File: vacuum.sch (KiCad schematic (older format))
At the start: 28 parts, among them J1 нагрузка, J2 нагрузка, J3 нагрузка, J4 геркон клапана 0, J5 геркон клапана 1, J6 геркон шибера 0, J7 геркон шибера 1, Q1 IRF740, Q2 IRF740, Q3 IRF740, SW1 Кнопка, SW2 Кнопка, SW3 Кнопка, SW4 Выключить автоматику

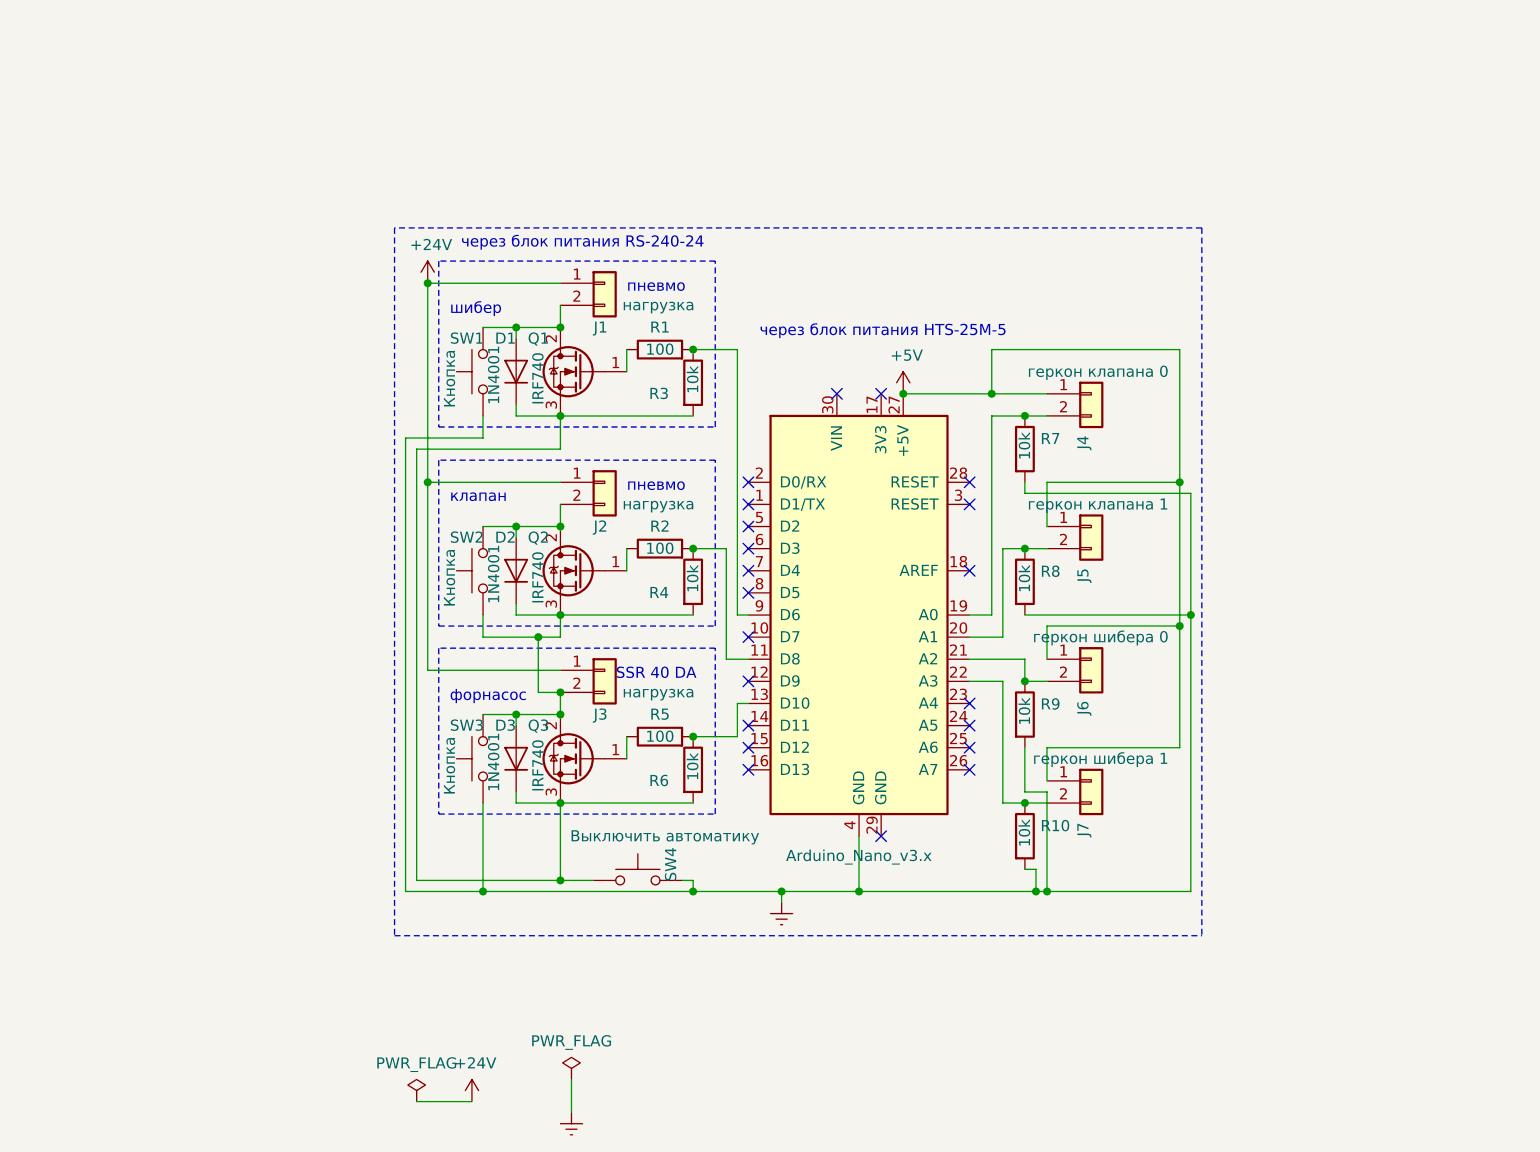
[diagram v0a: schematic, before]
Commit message: OPTRON added to valves and pump
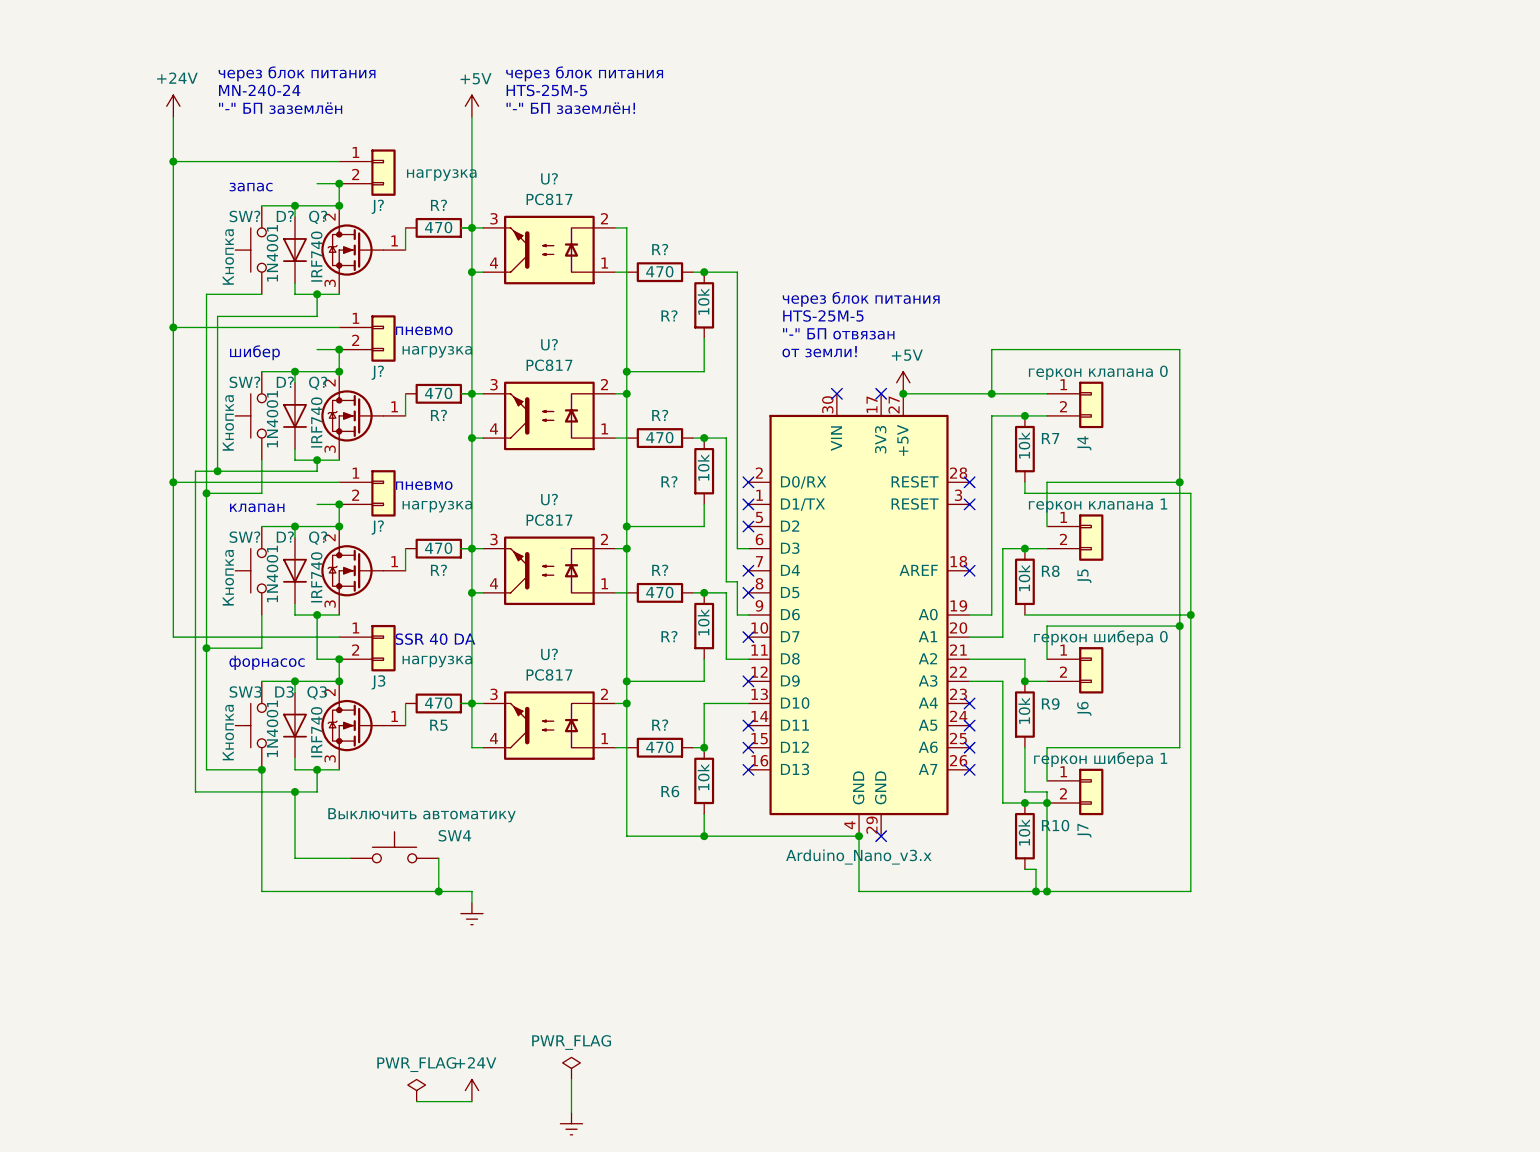
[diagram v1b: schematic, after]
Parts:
- removed D1, D2: 1N4001, Diode_THT:D_DO-41_SOD81_P10.16mm_Horizontal, symbol Diode:1N4001
- removed J1, J2: нагрузка, Connector_Phoenix_MSTB:PhoenixContact_MSTBV_2,5_2-GF_1x02_P5.00mm_Vertical_ThreadedFlange, symbol Connector_Generic:Conn_01x02
- removed Q1, Q2: IRF740, Package_TO_SOT_THT:TO-220-3_Vertical, symbol Transistor_FET:IRF740
- removed R1, R2: 100, Resistor_THT:R_Axial_DIN0207_L6.3mm_D2.5mm_P7.62mm_Horizontal, symbol Device:R
- removed R3, R4: 10k, Resistor_THT:R_Axial_DIN0309_L9.0mm_D3.2mm_P12.70mm_Horizontal, symbol Device:R
- removed SW1, SW2: Кнопка, Button_Switch_THT:SW_PUSH_6mm_H5mm, symbol Switch:SW_Push
- added D? (x3): 1N4001, Diode_THT:D_DO-41_SOD81_P10.16mm_Horizontal, symbol Diode:1N4001
- added J? (x3): нагрузка, Connector_Phoenix_MSTB:PhoenixContact_MSTBV_2,5_2-GF_1x02_P5.00mm_Vertical_ThreadedFlange, symbol Connector_Generic:Conn_01x02
- added Q? (x3): IRF740, Package_TO_SOT_THT:TO-220-3_Vertical, symbol Transistor_FET:IRF740
- added R? (x7): 470, Resistor_THT:R_Axial_DIN0207_L6.3mm_D2.5mm_P7.62mm_Horizontal, symbol Device:R
- added R? (x3): 10k, Resistor_THT:R_Axial_DIN0309_L9.0mm_D3.2mm_P12.70mm_Horizontal, symbol Device:R
- added SW? (x3): Кнопка, Button_Switch_THT:SW_PUSH_6mm_H5mm, symbol Switch:SW_Push
- added U? (x4): PC817, Package_DIP:DIP-4_W7.62mm, symbol Isolator:PC817
- R5: value 100 -> 470
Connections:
- wire segments 105 -> 177
- no-connect marks 21 -> 20
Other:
- note added: "запас"
- note added: "через блок питания \nHTS-25M-5\n"-" БП заземлён!"
- note added: "через блок питания \nHTS-25M-5\n"-" БП отвязан \nот земли!"
- note added: "через блок питания\nMN-240-24\n"-" БП заземлён"
- note removed: "через блок питания HTS-25M-5"
- note removed: "через блок питания RS-240-24"
- moved on the sheet: D3, J3, Q3, R5, R6, SW3, SW4

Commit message: OPTRON added to the reed switches, some reserve relay and reed switches added
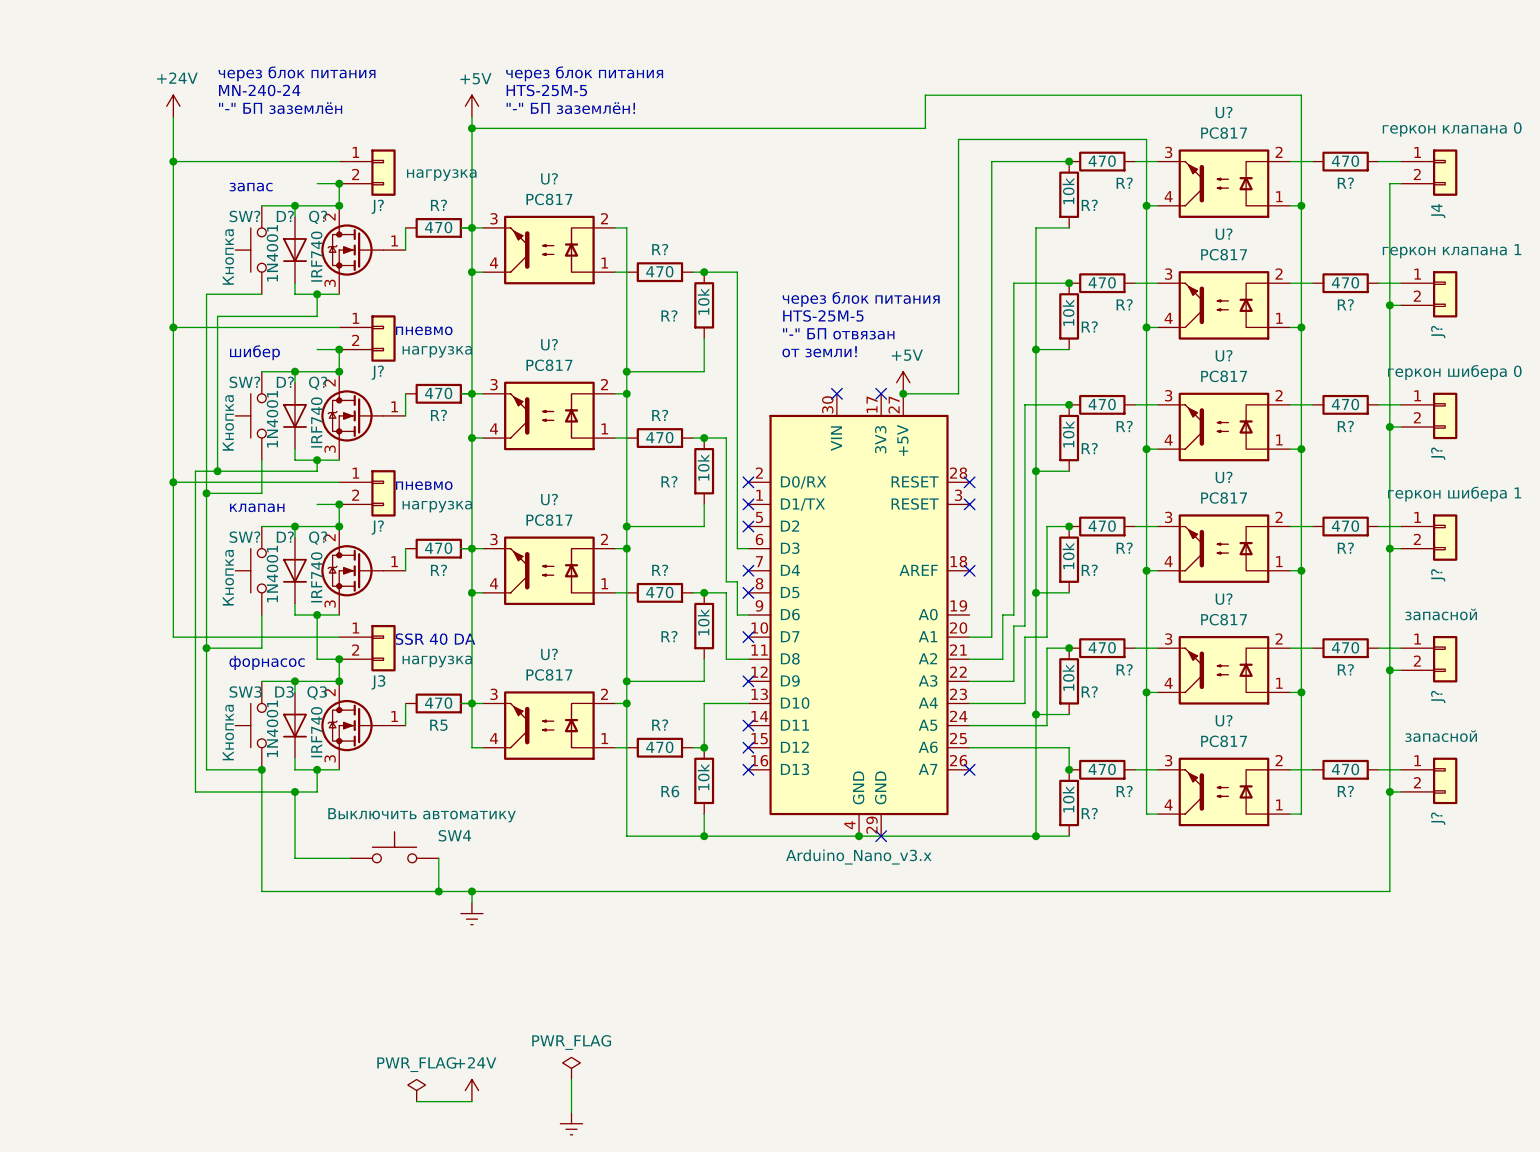
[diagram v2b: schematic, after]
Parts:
- removed J5: геркон клапана 1, Connector_Phoenix_MSTB:PhoenixContact_MSTBV_2,5_2-GF_1x02_P5.00mm_Vertical_ThreadedFlange, symbol Connector_Generic:Conn_01x02
- removed J6: геркон шибера 0, Connector_Phoenix_MSTB:PhoenixContact_MSTBV_2,5_2-GF_1x02_P5.00mm_Vertical_ThreadedFlange, symbol Connector_Generic:Conn_01x02
- removed J7: геркон шибера 1, Connector_Phoenix_MSTB:PhoenixContact_MSTBV_2,5_2-GF_1x02_P5.00mm_Vertical_ThreadedFlange, symbol Connector_Generic:Conn_01x02
- removed R10, R7, R8, R9: 10k, Resistor_THT:R_Axial_DIN0309_L9.0mm_D3.2mm_P12.70mm_Horizontal, symbol Device:R
- added J?: геркон клапана 1, Connector_Phoenix_MSTB:PhoenixContact_MSTBV_2,5_2-GF_1x02_P5.00mm_Vertical_ThreadedFlange, symbol Connector_Generic:Conn_01x02
- added J?: геркон шибера 0, Connector_Phoenix_MSTB:PhoenixContact_MSTBV_2,5_2-GF_1x02_P5.00mm_Vertical_ThreadedFlange, symbol Connector_Generic:Conn_01x02
- added J?: геркон шибера 1, Connector_Phoenix_MSTB:PhoenixContact_MSTBV_2,5_2-GF_1x02_P5.00mm_Vertical_ThreadedFlange, symbol Connector_Generic:Conn_01x02
- added J? (x2): запасной, Connector_Phoenix_MSTB:PhoenixContact_MSTBV_2,5_2-GF_1x02_P5.00mm_Vertical_ThreadedFlange, symbol Connector_Generic:Conn_01x02
- added R? (x6): 10k, Resistor_THT:R_Axial_DIN0309_L9.0mm_D3.2mm_P12.70mm_Horizontal, symbol Device:R
- added R? (x12): 470, Resistor_THT:R_Axial_DIN0207_L6.3mm_D2.5mm_P7.62mm_Horizontal, symbol Device:R
- added U? (x6): PC817, Package_DIP:DIP-4_W7.62mm, symbol Isolator:PC817
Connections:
- wire segments 177 -> 231
- no-connect marks 20 -> 17
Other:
- moved on the sheet: J4

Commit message: common - for power supply added, terminals to power supply added
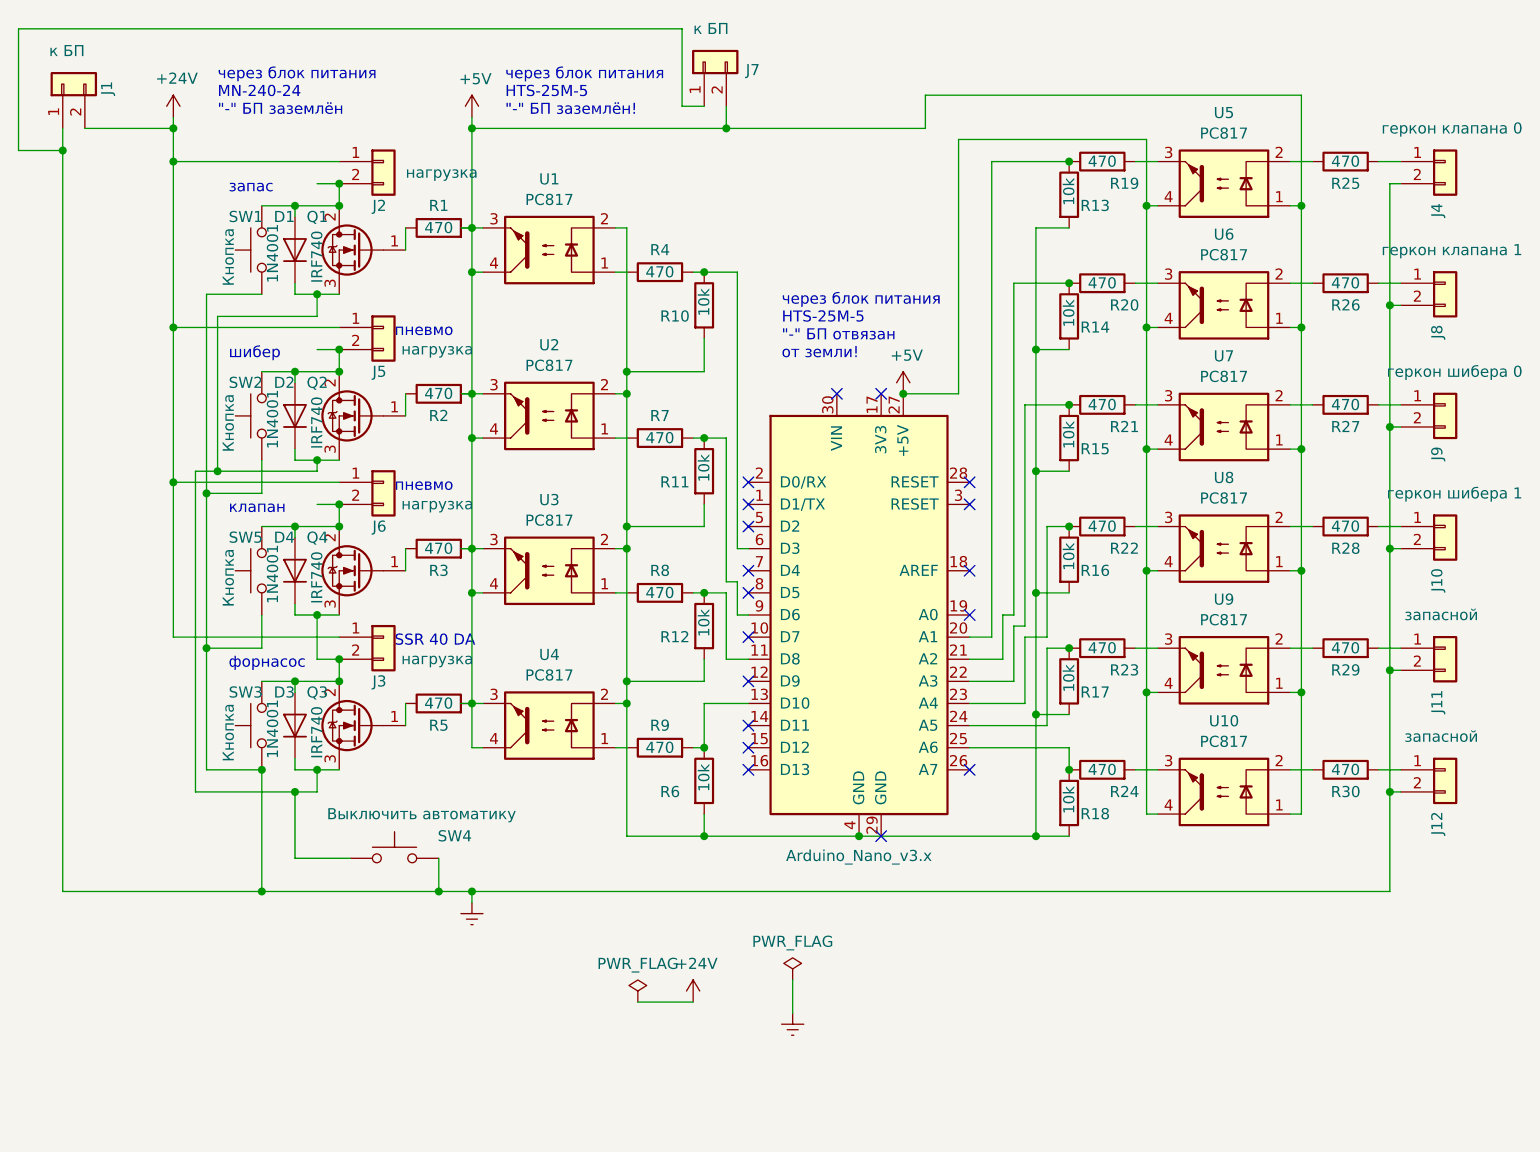
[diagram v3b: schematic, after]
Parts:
- added J1, J7: к БП, Connector_Phoenix_MSTB:PhoenixContact_MSTBV_2,5_2-GF_1x02_P5.00mm_Vertical_ThreadedFlange, symbol Connector_Generic:Conn_01x02
- gave numbers to parts that had none: 55
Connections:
- wire segments 231 -> 243
- no-connect marks 17 -> 18
